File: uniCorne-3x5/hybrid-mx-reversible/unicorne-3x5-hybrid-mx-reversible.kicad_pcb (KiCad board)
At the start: 2 copper layers, 114.7 x 91.4 mm, 93 parts, among them J1 MJ-4PP-9, J2 Nice!View, J3 Conn_01x02, J4 Conn_01x03, SW1 SW_MX_HS, SW10 SW_MX_HS, SW11 SW_MX_HS, SW12 SW_MX_HS, SW13 SW_MX_HS, SW14 SW_MX_HS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

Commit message: fixed 3x5
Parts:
- removed JP12, JP13, JP14, JP15: , TB2086_MISC:SolderJumper-2_P1.3mm_Open_TrianglePad1.0x1.2mm
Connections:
- U1 pad 24: RAW -> BAT+
- U1 pad 25: D+/B+ -> BAT+
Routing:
- net RAW: track 11.9 -> 0.00 mm, vias 1 -> 0
- net BAT+: track 13.4 -> 19.8 mm
- net D+/B+: track 1.91 -> 0.00 mm
- net col4: track 151.5 -> 152.1 mm

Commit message: fixed 3x6
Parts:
- moved JP11 3.17 mm to (172.9, 67.0), turned to -90 degrees
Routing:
- net col3: track 152.6 -> 149.9 mm
- net B-/D-: track 18.2 -> 20.6 mm
- net col2: track 186.0 -> 184.5 mm
- net col1: track 153.6 -> 152.1 mm
- net col0: track 174.3 -> 173.0 mm
- net GND: track 22.9 -> 24.2 mm, vias 15 -> 16
- net col4: track 152.1 -> 151.1 mm

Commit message: KiCAD 8
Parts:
- D1, D10, D11, D12, D13, D14, D15, D16, D17, D18, D2, D3, D4, D5, D6, D7, D8, D9: moved to F.Cu

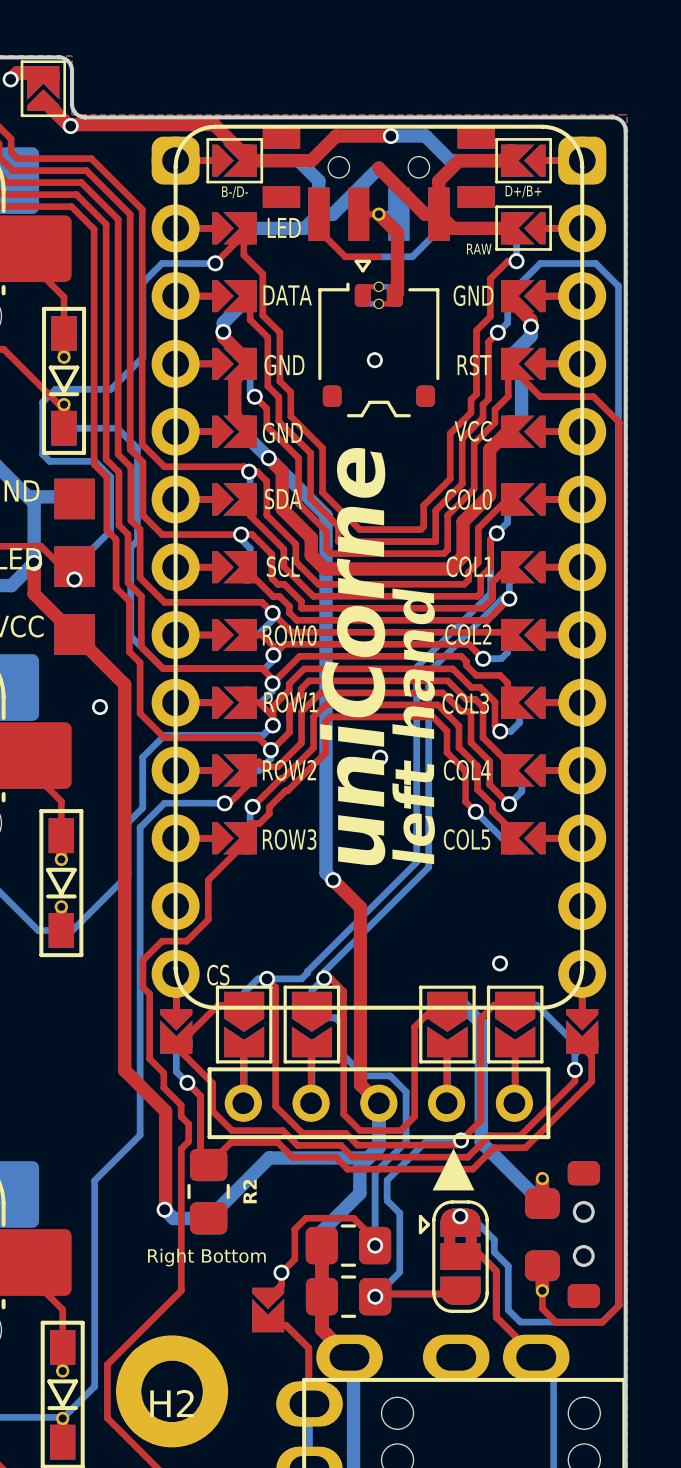
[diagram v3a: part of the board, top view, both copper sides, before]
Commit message: fixed SDA/SCL shorted
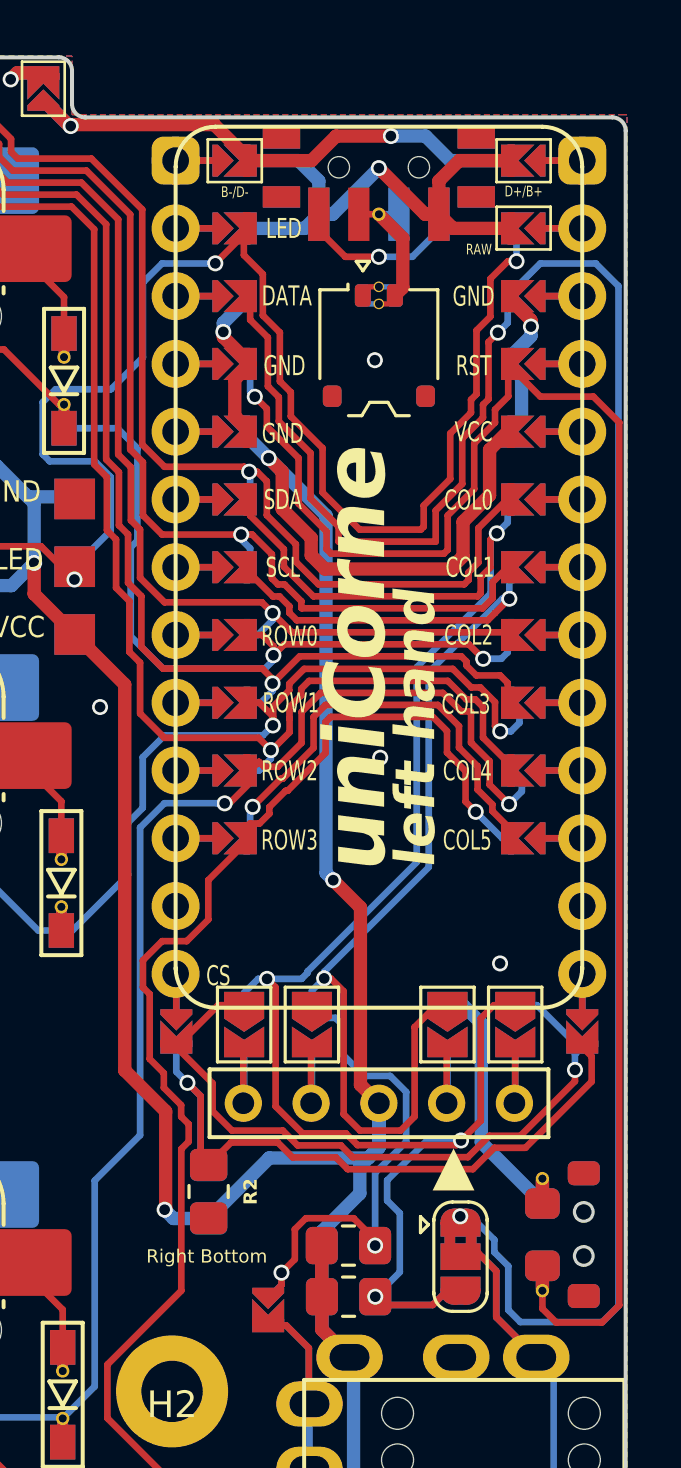
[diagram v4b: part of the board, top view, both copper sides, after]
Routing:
- net SDA: track 70.8 -> 71.3 mm
- net unconnected-(PSW1-C-Pad3)_1: vias 0 -> 1
- net BAT+: vias 0 -> 1
